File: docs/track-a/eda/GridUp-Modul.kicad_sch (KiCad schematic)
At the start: 54 parts, among them J1 İç ihtiyaç L / N / PE, J2 CT L1, J3 CT L2, J4 CT L3, J5 CT nötr, J6 Genişleme 2×5, J7 RS-485 klemens B / GND / A, J8 SMA panel, J9 Servis USB/UART0, SW1 Reset, U1 ESP32-S3-WROOM-1U-N8, U2 MLX90640ESF-BAA, U3 SHT31-DIS-B, U4 MAX3485, U5 RAC05-05SK/277, U6 AP7361C-33E 3,3 V / 1 A, U7 TPS61099 4,6 V

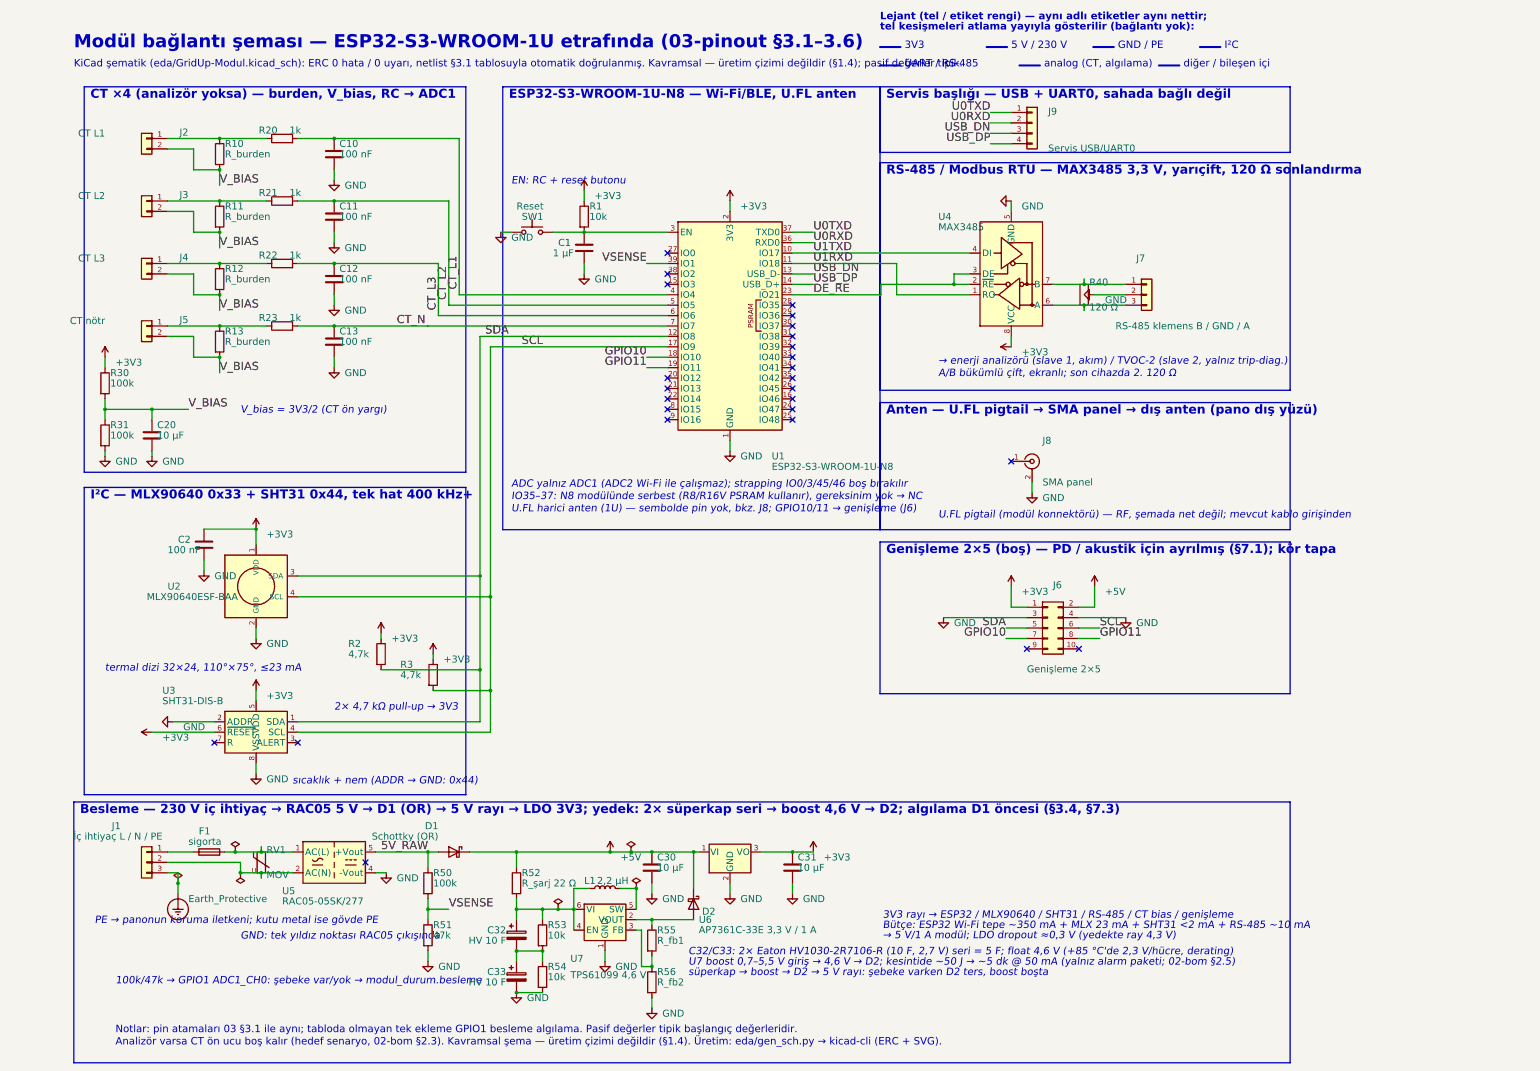
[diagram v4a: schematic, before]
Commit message: İZ A: SVG gözden geçirme turu 1 — 02: boost U7 + L MLX90640'ın arkasından X 46–49 / Y 31,5–38'e taşındı (sensör ekseninde parça yoktu ama çizimde dairenin içine düşüyordu), etiketlere zemin renkli arka plan (svgkit halo: Arial metriğiyle dikdörtgen, kesikli çerçeve üstünde okunur), MLX künyesi dairenin üstüne, 'D1 (OR) üst / D2 alt' tek etiket, R_şarj 22 Ω sağa, EN etiketi RC üstüne; tüm SVG'lerde em dash kaldırıldı (' / ' ayracı); Fusion: model script'leri başta timeline'ı temizliyor (eski zincir 'Kapak (1)', 'Gövde15–22' kopyalarını üretiyordu) → Kutu v10 4 gövde kopyasız, PCB v6 timeline 386→112, Montaj v12, Pano v16 (plaka gövdeye birleşik); f3d/step/views/02-03-04-09 SVG yeniden üretildi
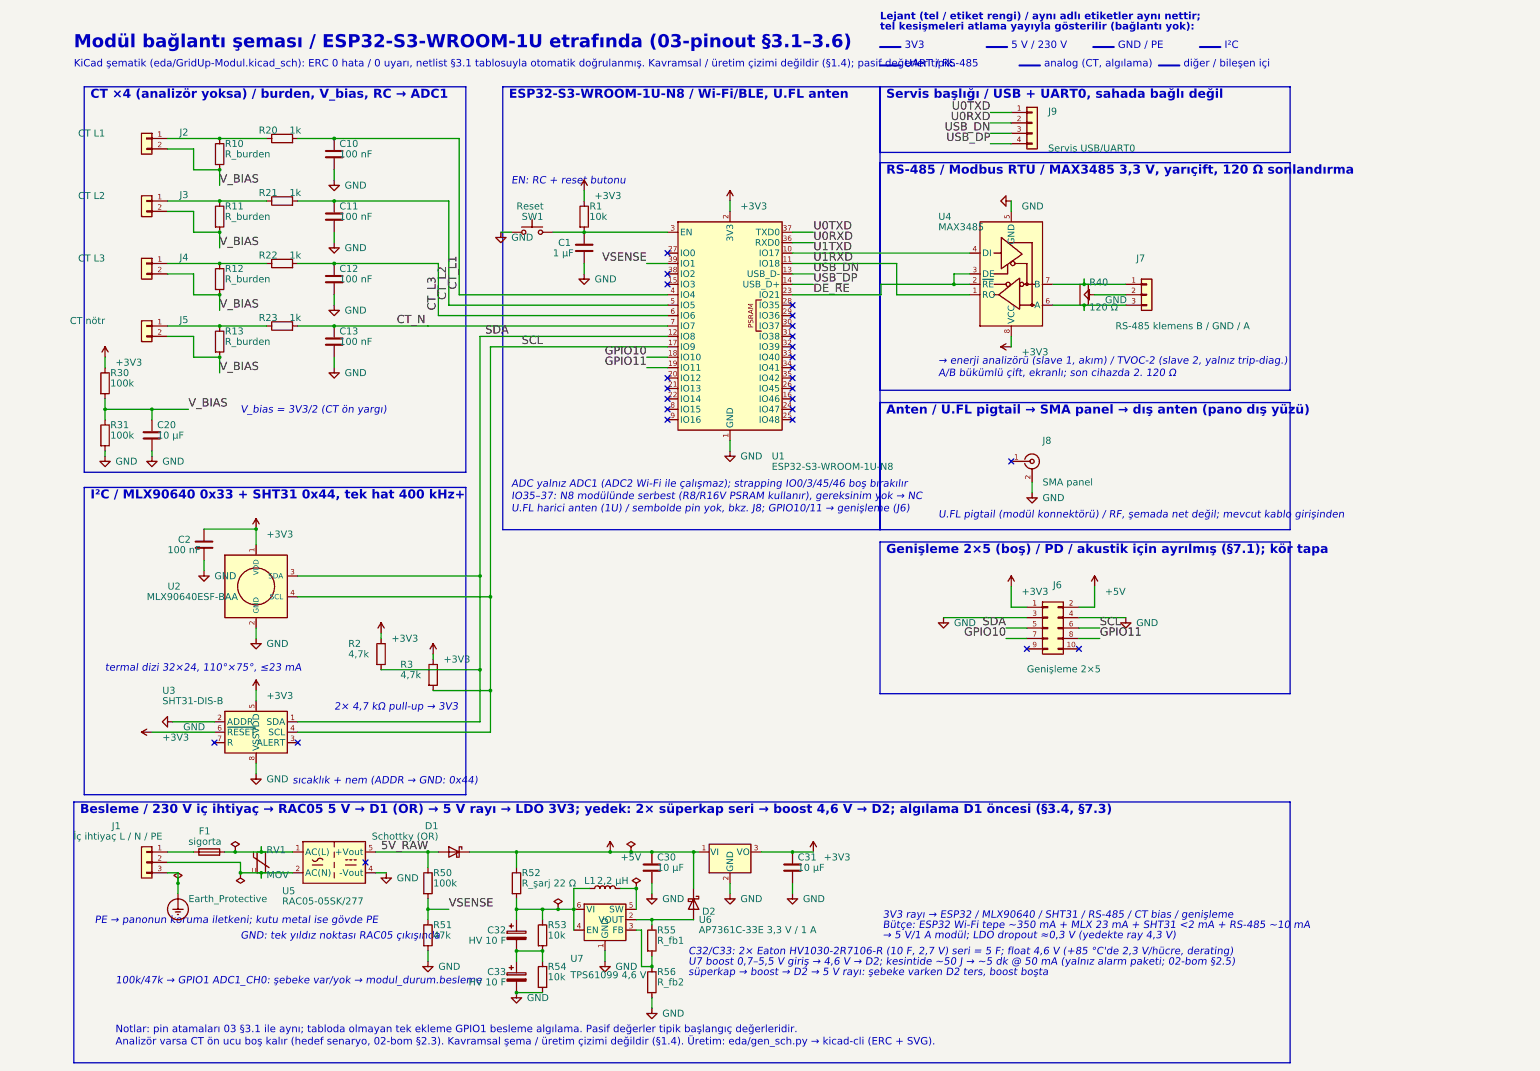
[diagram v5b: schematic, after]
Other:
- note added: "Analizör varsa CT ön ucu boş kalır (hedef senaryo, 02-bom §2.3). Kavramsal şema / üretim çizimi değildir (§1.4). Üretim: eda/gen_sch.py → kicad-cli (ERC + SVG)."
- note added: "Anten / U.FL pigtail → SMA panel → dış anten (pano dış yüzü)"
- note added: "Besleme / 230 V iç ihtiyaç → RAC05 5 V → D1 (OR) → 5 V rayı → LDO 3V3; yedek: 2× süperkap seri → boost 4,6 V → D2; algılama D1 öncesi (§3.4, §7.3)"
- note added: "CT ×4 (analizör yoksa) / burden, V_bias, RC → ADC1"
- note added: "ESP32-S3-WROOM-1U-N8 / Wi-Fi/BLE, U.FL anten"
- note added: "Genişleme 2×5 (boş) / PD / akustik için ayrılmış (§7.1); kör tapa"
- note added: "I²C / MLX90640 0x33 + SHT31 0x44, tek hat 400 kHz+"
- note added: "KiCad şematik (eda/GridUp-Modul.kicad_sch): ERC 0 hata / 0 uyarı, netlist §3.1 tablosuyla otomatik doğrulanmış. Kavramsal / üretim çizimi değildir (§1.4); pasif değerler tipik."
- note added: "Lejant (tel / etiket rengi) / aynı adlı etiketler aynı nettir;"
- note added: "Modül bağlantı şeması / ESP32-S3-WROOM-1U etrafında (03-pinout §3.1–3.6)"
- note added: "RS-485 / Modbus RTU / MAX3485 3,3 V, yarıçift, 120 Ω sonlandırma"
- note added: "Servis başlığı / USB + UART0, sahada bağlı değil"
- note added: "U.FL harici anten (1U) / sembolde pin yok, bkz. J8; GPIO10/11 → genişleme (J6)"
- note added: "U.FL pigtail (modül konnektörü) / RF, şemada net değil; mevcut kablo girişinden"
- note removed: "Analizör varsa CT ön ucu boş kalır (hedef senaryo, 02-bom §2.3). Kavramsal şema — üretim çizimi değildir (§1.4). Üretim: eda/gen_sch.py → kicad-cli (ERC + SVG)."
- note removed: "Anten — U.FL pigtail → SMA panel → dış anten (pano dış yüzü)"
- note removed: "Besleme — 230 V iç ihtiyaç → RAC05 5 V → D1 (OR) → 5 V rayı → LDO 3V3; yedek: 2× süperkap seri → boost 4,6 V → D2; algılama D1 öncesi (§3.4, §7.3)"
- note removed: "CT ×4 (analizör yoksa) — burden, V_bias, RC → ADC1"
- note removed: "ESP32-S3-WROOM-1U-N8 — Wi-Fi/BLE, U.FL anten"
- note removed: "Genişleme 2×5 (boş) — PD / akustik için ayrılmış (§7.1); kör tapa"
- note removed: "I²C — MLX90640 0x33 + SHT31 0x44, tek hat 400 kHz+"
- note removed: "KiCad şematik (eda/GridUp-Modul.kicad_sch): ERC 0 hata / 0 uyarı, netlist §3.1 tablosuyla otomatik doğrulanmış. Kavramsal — üretim çizimi değildir (§1.4); pasif değerler tipik."
- note removed: "Lejant (tel / etiket rengi) — aynı adlı etiketler aynı nettir;"
- note removed: "Modül bağlantı şeması — ESP32-S3-WROOM-1U etrafında (03-pinout §3.1–3.6)"
- note removed: "RS-485 / Modbus RTU — MAX3485 3,3 V, yarıçift, 120 Ω sonlandırma"
- note removed: "Servis başlığı — USB + UART0, sahada bağlı değil"
- note removed: "U.FL harici anten (1U) — sembolde pin yok, bkz. J8; GPIO10/11 → genişleme (J6)"
- note removed: "U.FL pigtail (modül konnektörü) — RF, şemada net değil; mevcut kablo girişinden"
- title: GridUp modül bağlantı şeması — ESP32-S3-WROOM-1U -> GridUp modül bağlantı şeması / ESP32-S3-WROOM-1U
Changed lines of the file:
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@@
 	(paper "User" 340 300)
 	(title_block
-		(title "GridUp modül bağlantı şeması — ESP32-S3-WROOM-1U")
+		(title "GridUp modül bağlantı şeması / ESP32-S3-WROOM-1U")
 		(date "2026-09-14")
 		(rev "1")
 		(company "Grid Up Hackathon / İZ A")
-		(comment 1 "Kavramsal şema — üretim çizimi değildir (karar kaydı §1.4). Pasif değerler tipik başlangıç değerleri.")
+		(comment 1 "Kavramsal şema / üretim çizimi değildir (karar kaydı §1.4). Pasif değerler tipik başlangıç değerleri.")
 		(comment 2 "Pin atamaları 03-pinout.md §3.1 ile aynı; kaynak: eda/gen_sch.py")
 	)
@@
 		)
 	)
-	(text "Modül bağlantı şeması — ESP32-S3-WROOM-1U etrafında (03-pinout §3.1–3.6)"
+	(text "Modül bağlantı şeması / ESP32-S3-WROOM-1U etrafında (03-pinout §3.1–3.6)"
 		(exclude_from_sim no)
 		(at 25.4 33 0)
@@
 		)
 	)
-	(text "KiCad şematik (eda/GridUp-Modul.kicad_sch): ERC 0 hata / 0 uyarı, netlist §3.1 tablosuyla otomatik doğrulanmış. Kavramsal — üretim çizimi değildir (§1.4); pasif değerler tipik."
+	(text "KiCad şematik (eda/GridUp-Modul.kicad_sch): ERC 0 hata / 0 uyarı, netlist §3.1 tablosuyla otomatik doğrulanmış. Kavramsal / üretim çizimi değildir (§1.4); pasif değerler tipik."
 		(exclude_from_sim no)
 		(at 25.4 37.5 0)
@@
 		)
 	)
-	(text "Lejant (tel / etiket rengi) — aynı adlı etiketler aynı nettir;"
+	(text "Lejant (tel / etiket rengi) / aynı adlı etiketler aynı nettir;"
 		(exclude_from_sim no)
 		(at 222 26 0)
@@
 		)
 	)
-	(text "ESP32-S3-WROOM-1U-N8 — Wi-Fi/BLE, U.FL anten"
+	(text "ESP32-S3-WROOM-1U-N8 / Wi-Fi/BLE, U.FL anten"
 		(exclude_from_sim no)
 		(at 131.5 45.2 0)
@@
 		)
 	)
-	(text "U.FL harici anten (1U) — sembolde pin yok, bkz. J8; GPIO10/11 → genişleme (J6)"
+	(text "U.FL harici anten (1U) / sembolde pin yok, bkz. J8; GPIO10/11 → genişleme (J6)"
 		(exclude_from_sim no)
 		(at 132.08 146 0)
@@
 		)
 	)
-	(text "CT ×4 (analizör yoksa) — burden, V_bias, RC → ADC1"
+	(text "CT ×4 (analizör yoksa) / burden, V_bias, RC → ADC1"
 		(exclude_from_sim no)
 		(at 29.44 45.2 0)
@@
 		)
 	)
-	(text "I²C — MLX90640 0x33 + SHT31 0x44, tek hat 400 kHz+"
+	(text "I²C / MLX90640 0x33 + SHT31 0x44, tek hat 400 kHz+"
 		(exclude_from_sim no)
 		(at 29.44 142.9 0)
@@
 		)
 	)
-	(text "Servis başlığı — USB + UART0, sahada bağlı değil"
+	(text "Servis başlığı / USB + UART0, sahada bağlı değil"
 		(exclude_from_sim no)
 		(at 223.5 45.2 0)
@@
 		)
 	)
-	(text "RS-485 / Modbus RTU — MAX3485 3,3 V, yarıçift, 120 Ω sonlandırma"
+	(text "RS-485 / Modbus RTU / MAX3485 3,3 V, yarıçift, 120 Ω sonlandırma"
 		(exclude_from_sim no)
 		(at 223.5 63.7 0)
@@
 		)
 	)
-	(text "Anten — U.FL pigtail → SMA panel → dış anten (pano dış yüzü)"
+	(text "Anten / U.FL pigtail → SMA panel → dış anten (pano dış yüzü)"
 		(exclude_from_sim no)
 		(at 223.5 122.2 0)
@@
 		)
 	)
-	(text "U.FL pigtail (modül konnektörü) — RF, şemada net değil; mevcut kablo girişinden"
+	(text "U.FL pigtail (modül konnektörü) / RF, şemada net değil; mevcut kablo girişinden"
 		(exclude_from_sim no)
 		(at 236.22 147.5 0)
@@
 		)
 	)
-	(text "Genişleme 2×5 (boş) — PD / akustik için ayrılmış (§7.1); kör tapa"
+	(text "Genişleme 2×5 (boş) / PD / akustik için ayrılmış (§7.1); kör tapa"
 		(exclude_from_sim no)
 		(at 223.5 156.2 0)
@@
 		(at 270.51 179.07)
 	)
-	(text "Besleme — 230 V iç ihtiyaç → RAC05 5 V → D1 (OR) → 5 V rayı → LDO 3V3; yedek: 2× süperkap seri → boost 4,6 V → D2; algılama D1 öncesi (§3.4, §7.3)"
+	(text "Besleme / 230 V iç ihtiyaç → RAC05 5 V → D1 (OR) → 5 V rayı → LDO 3V3; yedek: 2× süperkap seri → boost 4,6 V → D2; algılama D1 öncesi (§3.4, §7.3)"
 		(exclude_from_sim no)
 		(at 26.9 219.6 0)
@@
 		)
 	)
-	(text "Analizör varsa CT ön ucu boş kalır (hedef senaryo, 02-bom §2.3). Kavramsal şema — üretim çizimi değildir (§1.4). Üretim: eda/gen_sch.py → kicad-cli (ERC + SVG)."
+	(text "Analizör varsa CT ön ucu boş kalır (hedef senaryo, 02-bom §2.3). Kavramsal şema / üretim çizimi değildir (§1.4). Üretim: eda/gen_sch.py → kicad-cli (ERC + SVG)."
 		(exclude_from_sim no)
 		(at 35.56 276 0)
